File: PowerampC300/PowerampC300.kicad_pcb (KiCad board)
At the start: 2 copper layers, 240 x 63 mm, 125 parts, among them J1 Conn_01x02, J2 Conn_01x02, J3 Conn_01x02, J4 Conn_01x01, J5 Conn_01x01, J6 Conn_01x01, J7 Conn_01x01, J8 Conn_01x02, J9 Conn_Coaxial, Q1 2N5551, Q10 MJE15033, Q11 MJE15032, Q12 MJE15032, Q13 2N5551, Q14 2N5401, Q15 MJE15032, Q16 MJE15033, Q17 MJL3281A, Q18 MJL1302A, Q19 MJL3281A, Q2 2N5551, Q20 MJL1302A, Q21 MJL3281A, Q22 MJL1302A, Q23 MJL3281A, Q24 MJL1302A, Q3 2N5401, Q4 2N5401, Q5 2N5551, Q6 2N5551, Q7 2N5551, Q8 2N5401

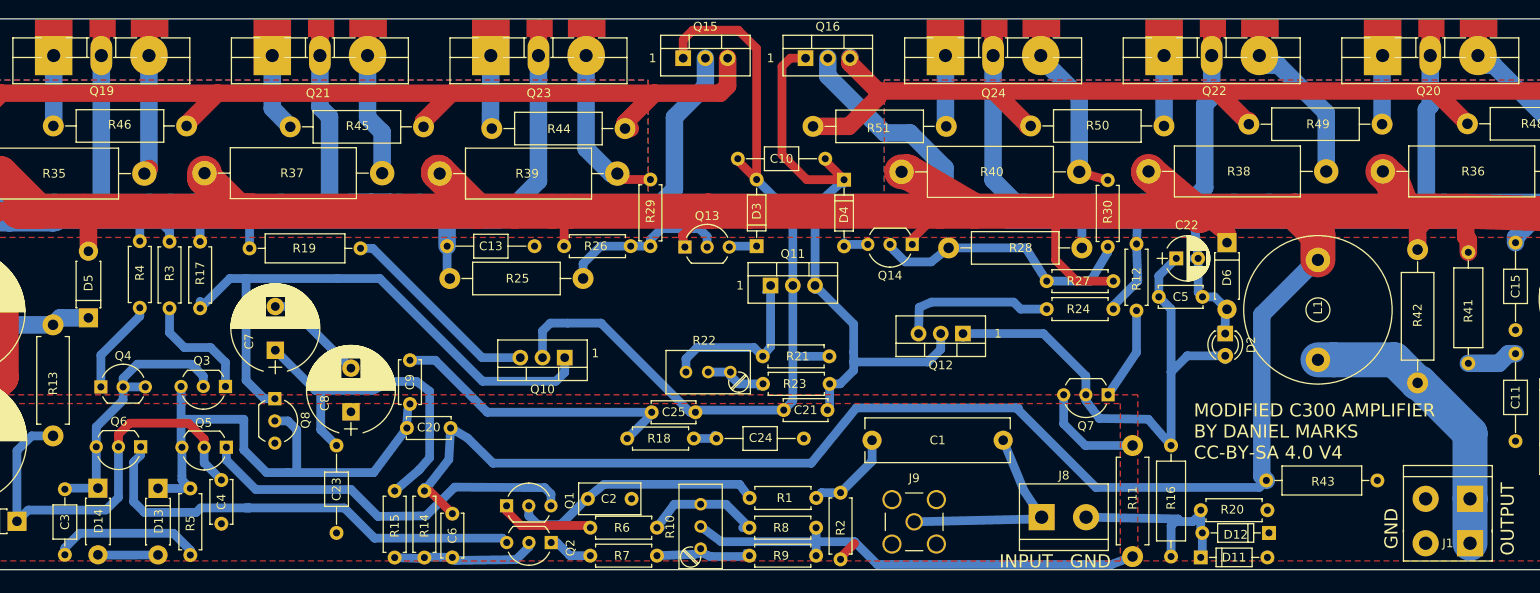
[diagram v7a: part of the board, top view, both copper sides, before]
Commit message: Changed to use optotriac shutoff of bias
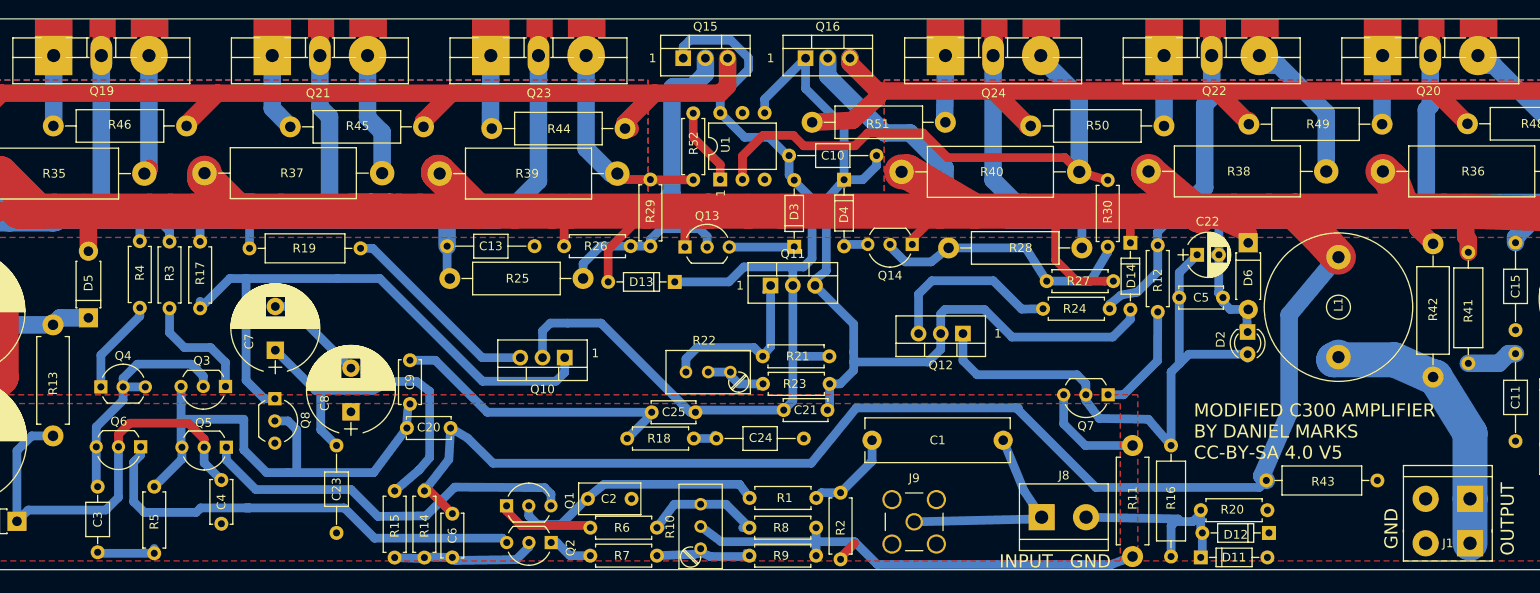
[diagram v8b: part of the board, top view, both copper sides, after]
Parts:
- added R52: 100R, Resistors_THT:R_Axial_DIN0207_L6.3mm_D2.5mm_P7.62mm_Horizontal, F.Cu at (138.2, 53.8)
- added U1: MOC3020M, Housings_DIP:DIP-6_W7.62mm, F.Cu at (141.2, 61.4)
- D13, D14: value NC -> 1N4148; footprint Diodes_THT:D_DO-41_SOD81_P7.62mm_Horizontal -> Diodes_THT:D_DO-35_SOD27_P7.62mm_Horizontal
- moved D14 121.4 mm to (188.2, 68.6)
- moved D13 63.7 mm to (136.0, 73.1), turned to 180 degrees
- moved C10 5.87 mm to (159.1, 58.6)
- moved D3 4.30 mm to (149.7, 69.1)
- moved R5 4.13 mm to (76.5, 96.5)
- moved C3 3.76 mm to (70.0, 104.0)
- moved D2 2.57 mm to (201.6, 78.8)
- moved R12 2.43 mm to (191.3, 68.9)
- moved D6 2.43 mm to (201.6, 68.6)
- moved C22 2.42 mm to (195.8, 70.0)
- moved L1 2.37 mm to (211.9, 81.7)
- moved C5 2.34 mm to (198.7, 74.9)
- moved R42 1.89 mm to (222.8, 68.7)
- moved R51 0.48 mm to (151.8, 54.8)
- moved R24 0.42 mm to (185.8, 76.2)
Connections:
- C10 pad 1: Net-(C10-Pad1) -> BIAS2
- C10 pad 2: Net-(C10-Pad2) -> BIAS1
- C21 pad 1: Net-(C10-Pad1) -> BIAS2
- C21 pad 2: Net-(C10-Pad2) -> BIAS1
- C25 pad 2: Net-(C10-Pad2) -> BIAS1
- D13 pad 1: Net-(C20-Pad1) -> BIAS1
- D13 pad 2: Net-(D13-Pad2) -> Net-(C20-Pad2)
- D14 pad 1: Net-(C3-Pad2) -> Net-(C20-Pad2)
- D14 pad 2: Net-(D13-Pad2) -> BIAS2
- D3 pad 2: Net-(C10-Pad2) -> BIAS1
- D4 pad 1: Net-(C10-Pad1) -> BIAS2
- Q10 pad 2: Net-(C10-Pad2) -> BIAS1
- Q11 pad 2: Net-(C10-Pad2) -> BIAS1
- Q11 pad 3: Net-(C10-Pad1) -> BIAS2
- Q12 pad 2: Net-(C10-Pad1) -> BIAS2
- Q15 pad 1: Net-(C10-Pad2) -> BIAS1
- Q16 pad 1: Net-(C10-Pad1) -> BIAS2
- R21 pad 2: Net-(C10-Pad2) -> BIAS1
- R23 pad 1: Net-(C10-Pad1) -> BIAS2
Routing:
- net BIAS1: track 0.00 -> 114.0 mm
- net BIAS2: track 0.00 -> 104.2 mm
- net Net-(C10-Pad2): track 98.6 -> 0.00 mm
- net Net-(C10-Pad1): track 72.1 -> 0.00 mm
- net Net-(Q24-Pad3): track 21.8 -> 66.9 mm
- net Net-(C20-Pad2): track 489.6 -> 507.0 mm
- net Net-(C3-Pad1): track 17.3 -> 7.16 mm
- net Net-(R52-Pad1): track 0.00 -> 8.86 mm
- net Net-(D13-Pad2): track 6.89 -> 0.00 mm
- net Net-(Q23-Pad3): track 23.0 -> 28.0 mm
- net +48V: track 334.8 -> 339.6 mm
- net Net-(D3-Pad1): track 3.16 -> 7.57 mm
- net Net-(C3-Pad2): track 31.9 -> 28.0 mm
- net Net-(C20-Pad1): track 59.3 -> 56.4 mm
- net Net-(C22-Pad1): track 62.8 -> 65.6 mm
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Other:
- board text added: "MODIFIED C300 AMPLIFIER BY DANIEL MARKS CC-BY-SA 4.0 V5"
- board text removed: "MODIFIED C300 AMPLIFIER BY DANIEL MARKS CC-BY-SA 4.0 V4"
